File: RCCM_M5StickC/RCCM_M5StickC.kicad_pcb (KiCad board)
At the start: 2 copper layers, 24.1 x 44.5 mm, 11 parts, among them CN1 Conn_02x04_Odd_Even, CN2 Conn_01x04, CN3 Conn_01x04, CN4 Conn_01x08

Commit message: Gerber change
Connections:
- S1 pad 6: G33 -> SD0
- S3 pad 6: SD0 -> G33
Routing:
- net SD0: track 13.0 -> 42.3 mm
- net G33: track 54.9 -> 40.5 mm
- net 3V3m: track 76.6 -> 69.0 mm
- net G00: track 64.6 -> 69.1 mm
- net G32: track 31.8 -> 36.2 mm
- net G26: track 61.9 -> 64.5 mm
- net GND: track 65.1 -> 63.5 mm
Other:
- board text added: "3V3"
- board text added: "GND"
- board text added: "RumiCar CM M5Stick-C"

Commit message: Gerber Update
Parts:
- added G***: LOGO, logos:ALGYAN2p5, B.Cu at (80.6, 64.1)
- added G***: LOGO, logos:RumiCar1_3p3, B.Cu at (77.2, 58.7)
- added G***: LOGO, logos:RumiCar2_3p3, B.Cu at (77.2, 66.4)
- added R1: R, Resistors_THT:R_Axial_DIN0207_L6.3mm_D2.5mm_P2.54mm_Vertical, F.Cu at (69.8, 55.2)
- added R2: R, Resistors_THT:R_Axial_DIN0207_L6.3mm_D2.5mm_P2.54mm_Vertical, F.Cu at (69.8, 74.3)
- moved CN2 5.72 mm to (81.3, 50.8), turned to 180 degrees
- moved CN3 5.72 mm to (81.3, 78.1), turned to 180 degrees
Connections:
- CN1 pad 6: G00 -> G26
- CN1 pad 8: G26 -> G00
- CN3 pad 3: G26 -> G00
- CN3 pad 4: G00 -> G26
- S1 pad 3: G00 -> G26
- S1 pad 4: G26 -> G00
- S1 pad 6: SD0 -> G33
- S2 pad 3: G00 -> G26
- S2 pad 4: G26 -> G00
- S3 pad 3: G00 -> G26
- S3 pad 4: G26 -> G00
- S3 pad 6: G33 -> SD0
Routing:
- net SD0: track 42.3 -> 13.6 mm
- net GND: track 63.5 -> 80.8 mm
- net G00: track 69.1 -> 56.3 mm
- net 3V3m: track 69.0 -> 76.0 mm
- net G32: track 36.2 -> 42.3 mm
- net G33: track 40.5 -> 41.3 mm
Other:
- board text added: "A.W. S.Inatama"

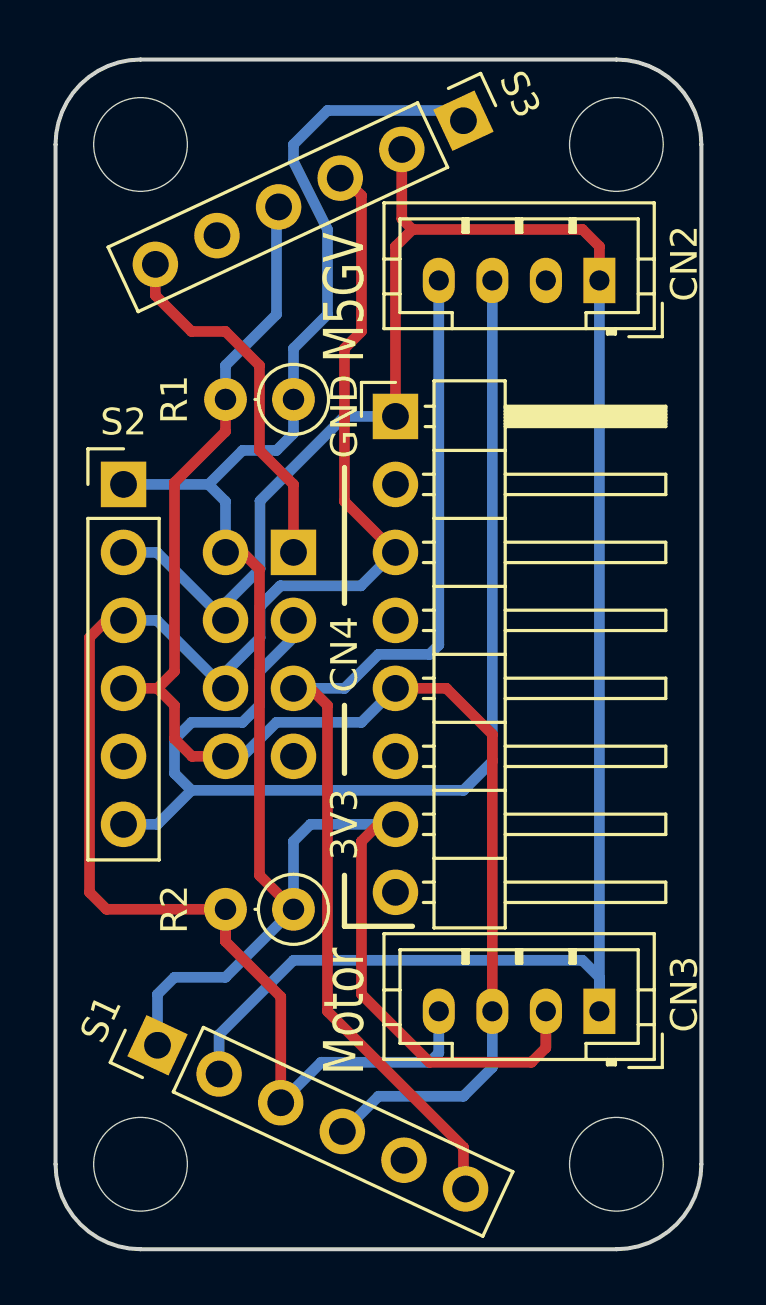
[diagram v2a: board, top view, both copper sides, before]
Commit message: SDx Update
(No:Pos:SDx:CNx:Nano:ESP32:M5S),
(S1:LEFT:SD0:CN1-5:No14:IO19:NC),
(S2:CEN:SD1:CN1-3:No15:IO18:G32),
(S3:RIGHT:SD2:CN1-1:No16:IO5:G33)
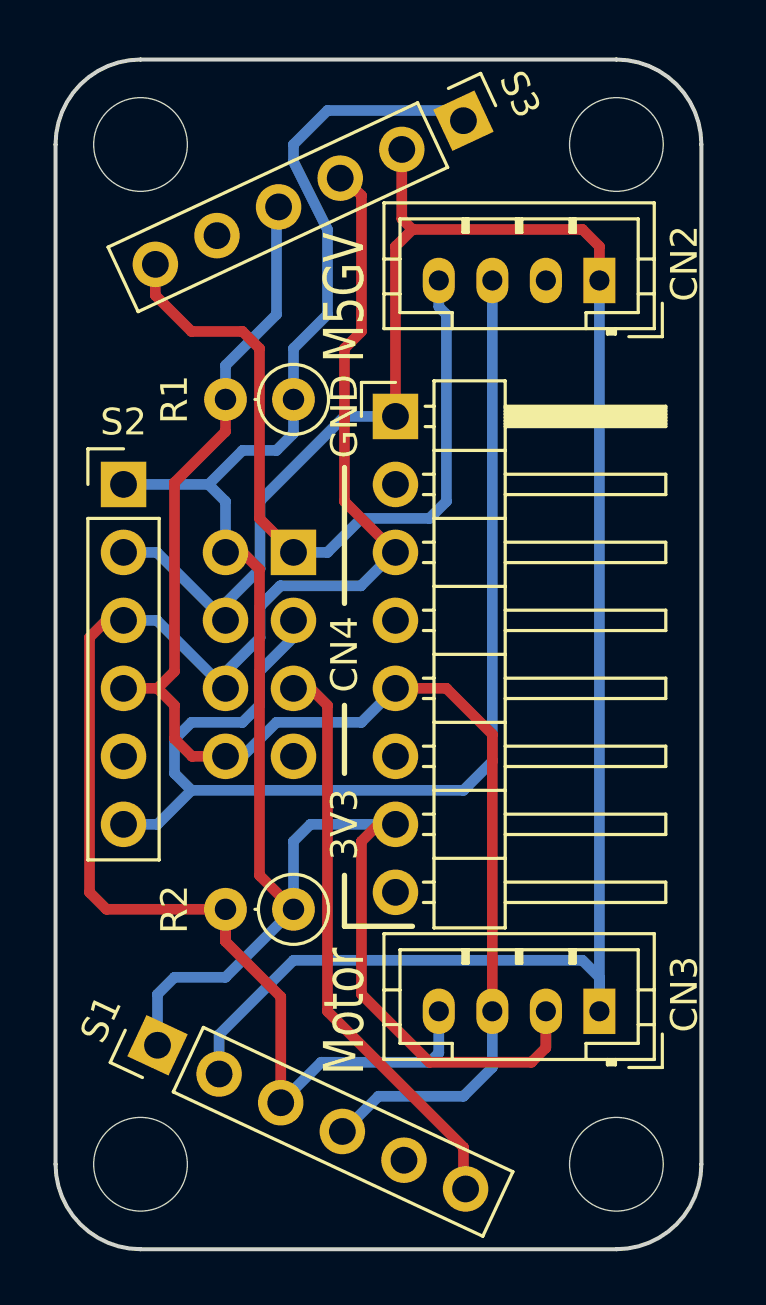
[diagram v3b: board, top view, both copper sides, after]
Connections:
- CN1 pad 1: SD0 -> G33
- CN1 pad 5: G33 -> SD0
- S1 pad 6: G33 -> SD0
- S3 pad 6: SD0 -> G33
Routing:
- net G33: track 41.3 -> 28.9 mm
- net SD0: track 13.6 -> 21.6 mm
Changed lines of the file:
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@@
     (thickness 1.6)
     (drawings 29)
-    (tracks 143)
+    (tracks 144)
     (zones 0)
     (modules 16)
@@
     )
     (pad 1 thru_hole rect (at 0 0 180) (size 1.7 1.7) (drill 1) (layers *.Cu *.Mask)
-      (net 1 SD0))
+      (net 5 G33))
     (pad 2 thru_hole oval (at 2.54 0 180) (size 1.7 1.7) (drill 1) (layers *.Cu *.Mask)
       (net 2 3V3m))
@@
       (net 4 GND))
     (pad 5 thru_hole oval (at 0 -5.08 180) (size 1.7 1.7) (drill 1) (layers *.Cu *.Mask)
-      (net 5 G33))
+      (net 1 SD0))
     (pad 6 thru_hole oval (at 2.54 -5.08 180) (size 1.7 1.7) (drill 1) (layers *.Cu *.Mask)
       (net 7 G26))
@@
     (pad 5 thru_hole oval (at 0 10.16 65) (size 1.7 1.7) (drill 1) (layers *.Cu *.Mask))
     (pad 6 thru_hole oval (at 0 12.7 65) (size 1.7 1.7) (drill 1) (layers *.Cu *.Mask)
-      (net 5 G33))
+      (net 1 SD0))
     (model ${KISYS3DMOD}/Pin_Headers.3dshapes/Pin_Header_Straight_1x06_Pitch2.54mm.wrl
       (at (xyz 0 0 0))
@@
     (pad 5 thru_hole oval (at 0 10.16 295) (size 1.7 1.7) (drill 1) (layers *.Cu *.Mask))
     (pad 6 thru_hole oval (at 0 12.7 295) (size 1.7 1.7) (drill 1) (layers *.Cu *.Mask)
-      (net 1 SD0))
+      (net 5 G33))
     (model ${KISYS3DMOD}/Pin_Headers.3dshapes/Pin_Header_Straight_1x06_Pitch2.54mm.wrl
       (at (xyz 0 0 0))
@@
     (arrow2b (pts (xy 60.96 29.845) (xy 62.086504 29.258579)))
   )
-  (segment (start 69.85 60.96) (end 69.85 58.42) (width 0.4) (layer F.Cu) (net 1))
-  (segment (start 64.689891 51.354891) (end 64.689891 50.198252) (width 0.4) (layer F.Cu) (net 1))
-  (segment (start 66.04 52.705) (end 64.689891 51.354891) (width 0.4) (layer F.Cu) (net 1))
-  (segment (start 67.31 52.705) (end 66.04 52.705) (width 0.4) (layer F.Cu) (net 1))
-  (segment (start 68.58 53.975) (end 67.31 52.705) (width 0.4) (layer F.Cu) (net 1))
-  (segment (start 68.58 57.15) (end 68.58 53.975) (width 0.4) (layer F.Cu) (net 1))
-  (segment (start 69.85 58.42) (end 68.58 57.15) (width 0.4) (layer F.Cu) (net 1))
+  (segment (start 69.85 66.04) (end 70.485 66.04) (width 0.4) (layer F.Cu) (net 1))
+  (segment (start 70.485 66.04) (end 71.12 66.675) (width 0.4) (layer F.Cu) (net 1))
+  (segment (start 76.2 83.185) (end 76.2 84.662143) (width 0.4) (layer F.Cu) (net 1))
+  (segment (start 71.12 78.105) (end 76.2 83.185) (width 0.4) (layer F.Cu) (net 1))
+  (segment (start 71.12 66.675) (end 71.12 78.105) (width 0.4) (layer F.Cu) (net 1))
   (segment (start 69.85 46.355) (end 69.85 45.72) (width 0.4) (layer B.Cu) (net 2))
   (segment (start 69.85 53.34) (end 71.12 52.07) (width 0.4) (layer B.Cu) (net 2))
@@
   (segment (start 80.645 48.895) (end 74.295 48.895) (width 0.4) (layer F.Cu) (net 4))
   (segment (start 81.28 49.53) (end 80.645 48.895) (width 0.4) (layer F.Cu) (net 4))
-  (segment (start 69.85 66.04) (end 70.485 66.04) (width 0.4) (layer F.Cu) (net 5))
-  (segment (start 70.485 66.04) (end 71.12 66.675) (width 0.4) (layer F.Cu) (net 5))
-  (segment (start 76.2 83.185) (end 76.2 84.662143) (width 0.4) (layer F.Cu) (net 5))
-  (segment (start 71.12 78.105) (end 76.2 83.185) (width 0.4) (layer F.Cu) (net 5))
-  (segment (start 71.12 66.675) (end 71.12 78.105) (width 0.4) (layer F.Cu) (net 5))
-  (segment (start 75.28 50.8) (end 75.28 64.42) (width 0.4) (layer B.Cu) (net 5) (status 10))
-  (segment (start 71.755 66.04) (end 69.85 66.04) (width 0.4) (layer B.Cu) (net 5) (status 20))
-  (segment (start 73.025 64.77) (end 71.755 66.04) (width 0.4) (layer B.Cu) (net 5))
-  (segment (start 74.93 64.77) (end 73.025 64.77) (width 0.4) (layer B.Cu) (net 5))
-  (segment (start 75.28 64.42) (end 74.93 64.77) (width 0.4) (layer B.Cu) (net 5))
+  (segment (start 69.85 60.96) (end 71.12 60.96) (width 0.4) (layer B.Cu) (net 5))
+  (segment (start 75.28 51.785) (end 75.28 50.8) (width 0.4) (layer B.Cu) (net 5))
+  (segment (start 75.565 52.07) (end 75.28 51.785) (width 0.4) (layer B.Cu) (net 5))
+  (segment (start 75.565 59.055) (end 75.565 52.07) (width 0.4) (layer B.Cu) (net 5))
+  (segment (start 74.93 59.69) (end 75.565 59.055) (width 0.4) (layer B.Cu) (net 5))
+  (segment (start 72.39 59.69) (end 74.93 59.69) (width 0.4) (layer B.Cu) (net 5))
+  (segment (start 71.12 60.96) (end 72.39 59.69) (width 0.4) (layer B.Cu) (net 5))
+  (segment (start 64.689891 50.198252) (end 64.689891 51.354891) (width 0.4) (layer F.Cu) (net 5))
+  (segment (start 68.58 59.69) (end 69.85 60.96) (width 0.4) (layer F.Cu) (net 5))
+  (segment (start 68.58 53.34) (end 68.58 59.69) (width 0.4) (layer F.Cu) (net 5))
+  (segment (start 67.945 52.705) (end 68.58 53.34) (width 0.4) (layer F.Cu) (net 5))
+  (segment (start 66.04 52.705) (end 67.945 52.705) (width 0.4) (layer F.Cu) (net 5))
+  (segment (start 64.689891 51.354891) (end 66.04 52.705) (width 0.4) (layer F.Cu) (net 5))
   (segment (start 67.31 55.245) (end 67.31 53.975) (width 0.4) (layer B.Cu) (net 6))
   (segment (start 69.215 52.07) (end 69.215 48.130286) (width 0.4) (layer B.Cu) (net 6))
